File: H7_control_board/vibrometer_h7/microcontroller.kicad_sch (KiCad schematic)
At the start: 34 parts, among them J2 Conn_ARM_SWD_TagConnect_TC203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, J3 Conn_01x04_Socket, Q201 BSS138, Q202 BSS138, SW201 SW_Push, U1 STM32H723VGTx, Y201 24MHz

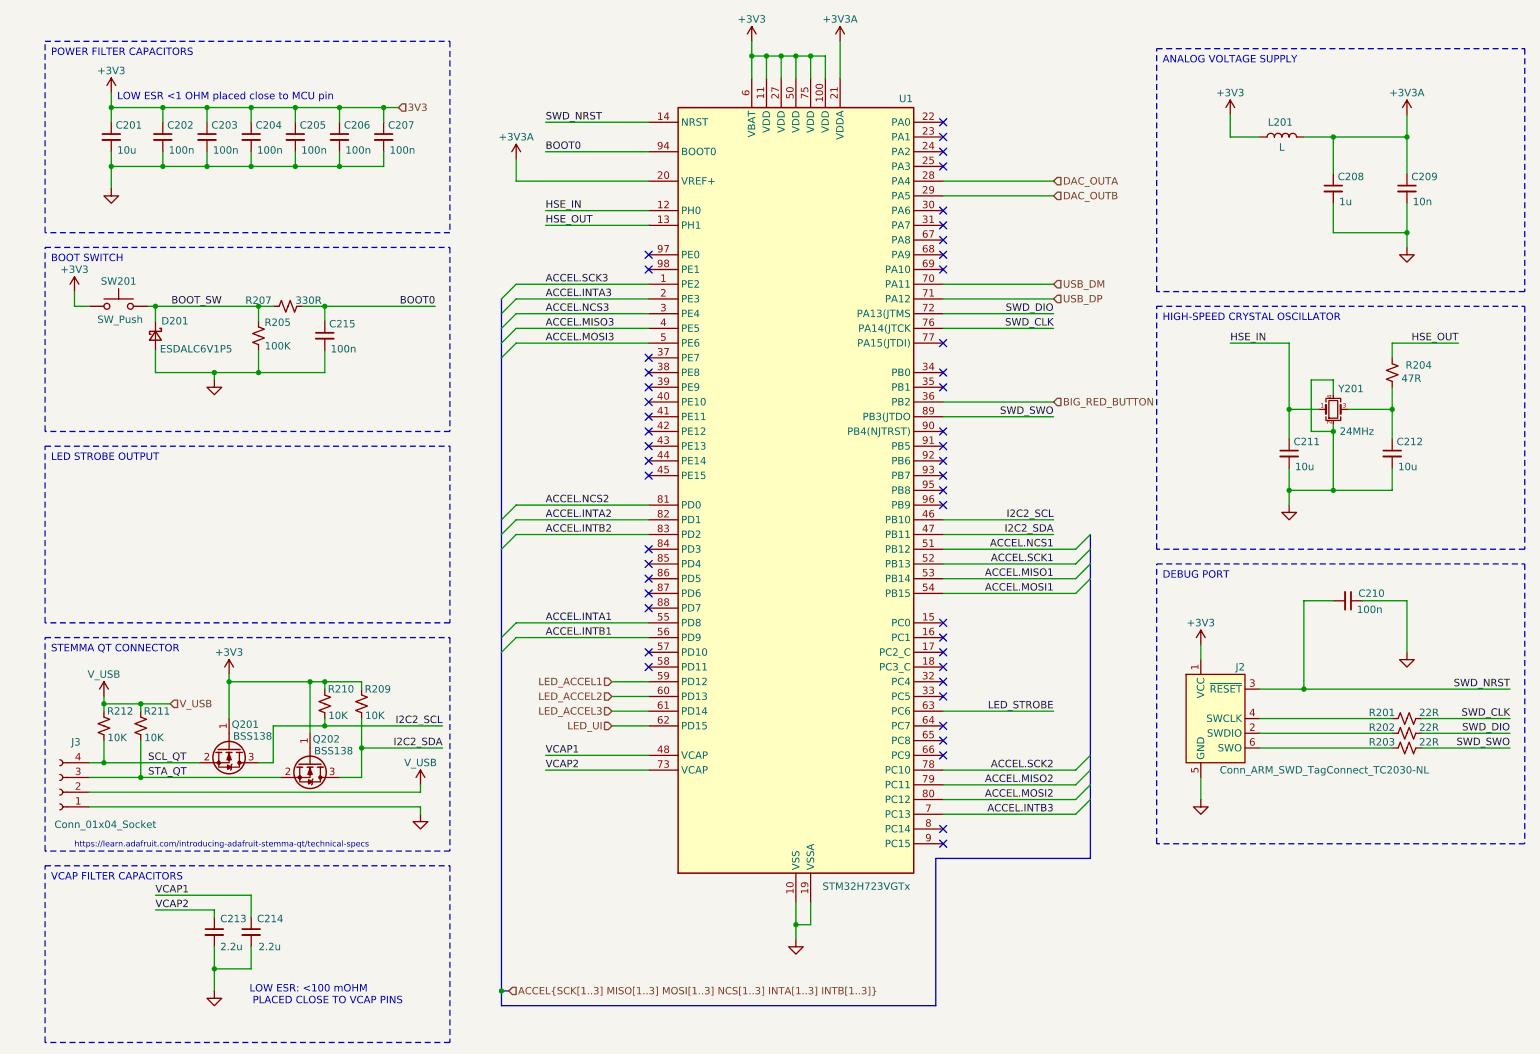
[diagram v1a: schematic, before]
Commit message: adding strobe light to board itself
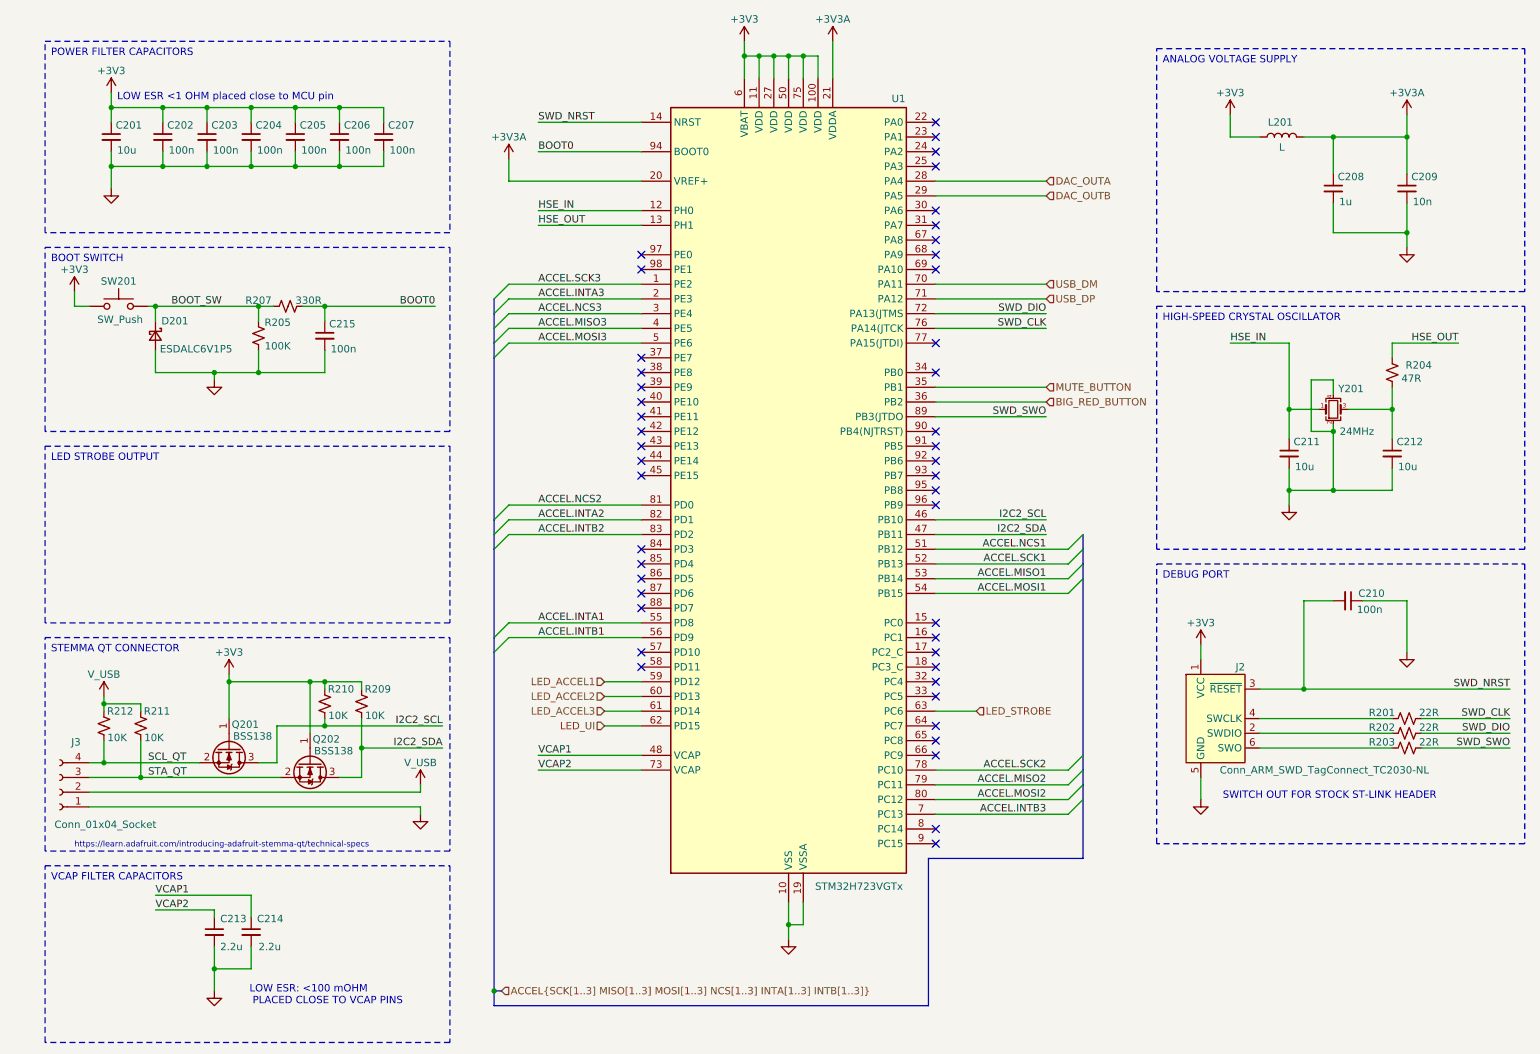
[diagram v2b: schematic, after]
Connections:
- net MUTE_BUTTON: now reaches U1.35 (PB1)
- no-connect marks 47 -> 46
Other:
- note added: "SWITCH OUT FOR STOCK ST-LINK HEADER"
- moved on the sheet: U1

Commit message: worked on audio output stuff, cleaned schematic
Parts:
- removed C210: 100n, symbol Device:C_Small
- removed J2: Conn_ARM_SWD_TagConnect_TC2030-NL, Connector:Tag-Connect_TC2030-IDC-NL_2x03_P1.27mm_Vertical, symbol Connector:Conn_ARM_SWD_TagConnect_TC2030-NL
- added C216, C5: 100n, symbol Device:C_Small
- added J4: Conn_ST_STDC14, symbol Connector:Conn_ST_STDC14
- C211, C212: value 10u -> 12p
- C213, C214: value 2.2u -> 2u2
- L201: value L -> 39n
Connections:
- net +3V3: now also J4.3 (VCC)
- net +3V3A: now also C216.1
- net GND: now also C216.2, C5.1, J4.11 (GNDDetect), J4.5 (GND), J4.7 (GND)
- net SWD_NRST: now also C5.2, J4.12 (~{RST})
- net MUTE_SIGNAL: now reaches U1.30 (PA6)
- net VCP_TX: now reaches U1.92 (PB6)
- net VCP_TX: now also J4.14 (VCP_TX)
- net VCP_RX: now reaches U1.93 (PB7)
- net VCP_RX: now also J4.13 (VCP_RX)
- net at R202.1: now also J4.4 (JTMS/SWDIO)
- net at R201.1: now also J4.6 (JCLK/SWCLK)
- net at R203.1: now also J4.8 (JTDO/SWO)
- net LED_ACCEL1 renamed LED_ACCEL
- net LED_ACCEL2: no longer names the net of U1.60 (PD13)
- net LED_ACCEL3: no longer names the net of U1.61 (PD14)
- no-connect marks 46 -> 47
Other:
- note added: "GPIO HEADER"
- note added: "ST-LINK DEBUG CONNECTOR"
- note removed: "SWITCH OUT FOR STOCK ST-LINK HEADER"
- moved on the sheet: C209

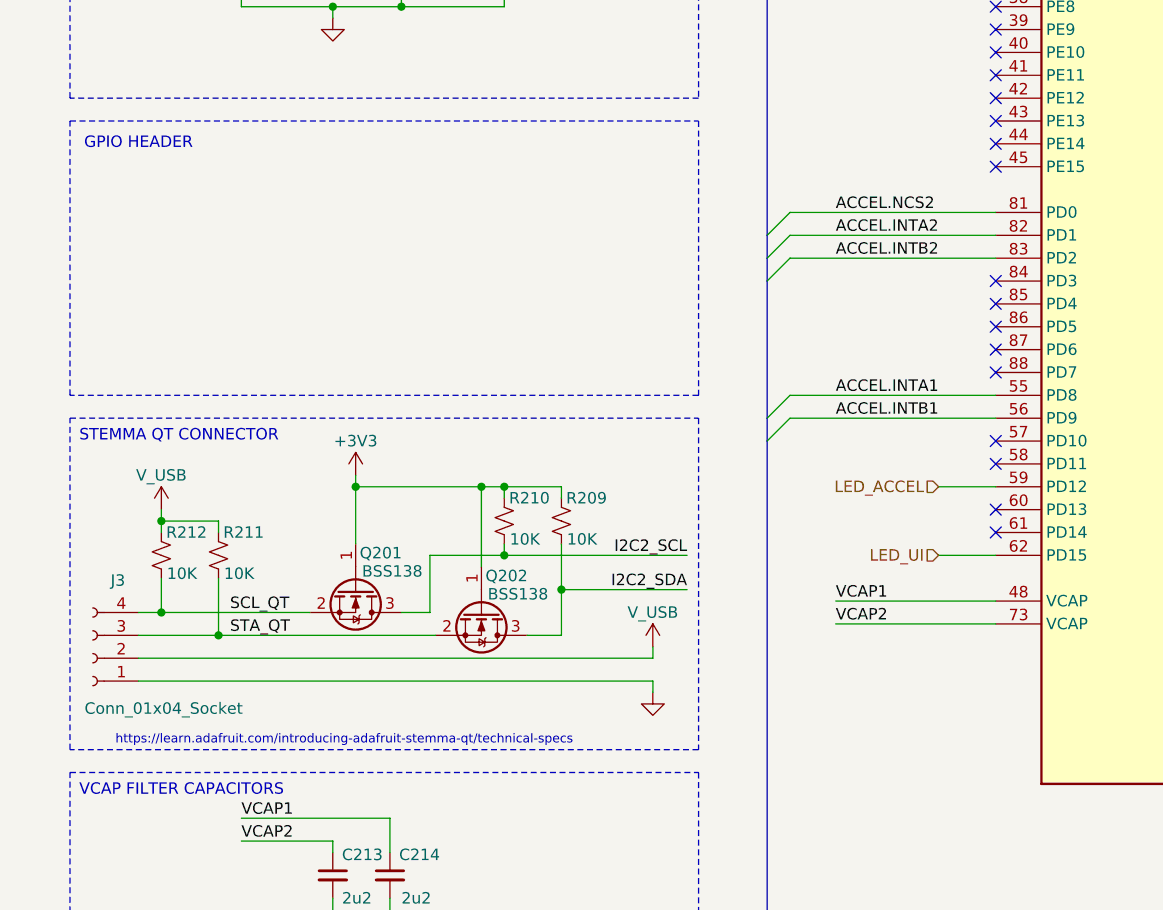
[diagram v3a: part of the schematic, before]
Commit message: met with john to go over schematic. made changes, got rid of some leds...
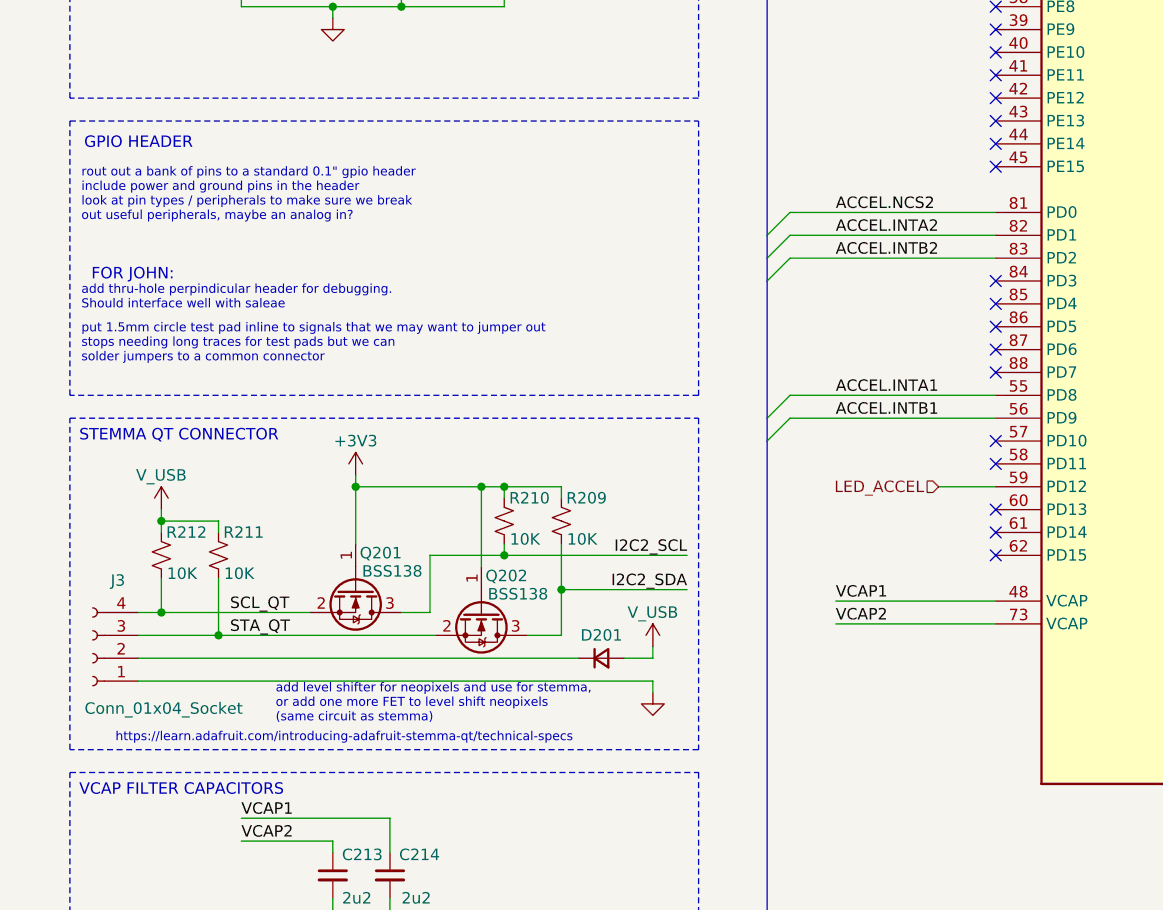
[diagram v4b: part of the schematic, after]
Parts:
- added D201: D_Small, symbol Device:D_Small
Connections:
- net V_USB: now also D201.2 (A); no longer J3.2 (Pin_2)
- net LED_UI: no longer names the net of U1.62 (PD15)
- new net: D201.1 (K), J3.2 (Pin_2)
- no-connect marks 47 -> 48
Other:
- note added: "FOR JOHN:"
- note added: "add level shifter for neopixels and use for stemma, or add one more FET to level shift neopixels (same circuit as stemma)"
- note added: "add thru-hole perpindicular header for debugging. Should interface well with saleae"
- note added: "put 1.5mm circle test pad inline to signals that we may want to jumper out stops needing long traces for test pads but we can solder jumpers to a common connector"
- note added: "rout out a bank of pins to a standard 0.1" gpio header include power and ground pins in the header look at pin types / peripherals to make sure we break out useful peripherals, maybe an analog in?"

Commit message: started part selection
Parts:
- C201, C202, C203, C204, C205, C206, C207, C208, C209, C211, C212, C213, C214, C215, C216, C5: footprint (none) -> Capacitor_SMD:C_0603_1608Metric
- SW201: footprint (none) -> Button_Switch_SMD:SW_Push_1P1T_XKB_TS-1187A; LCSC (none) -> C318884

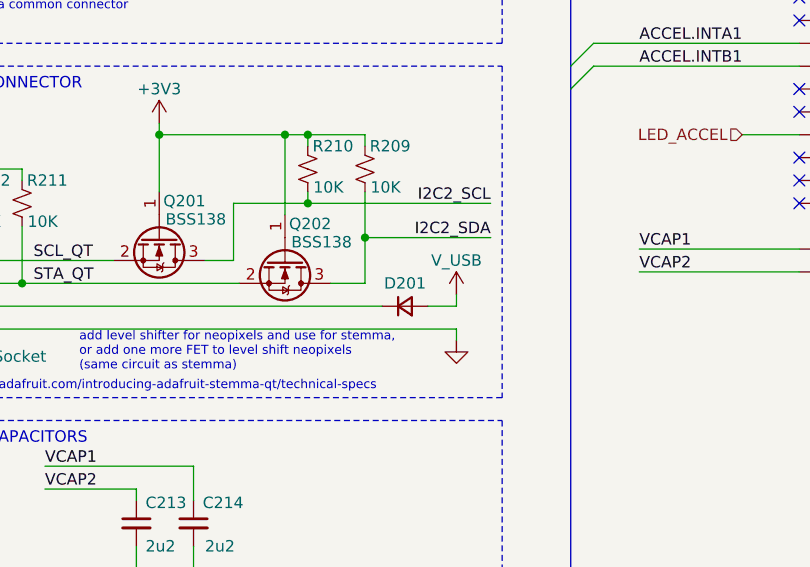
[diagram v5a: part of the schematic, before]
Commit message: component selection, headphone amp circuit specs
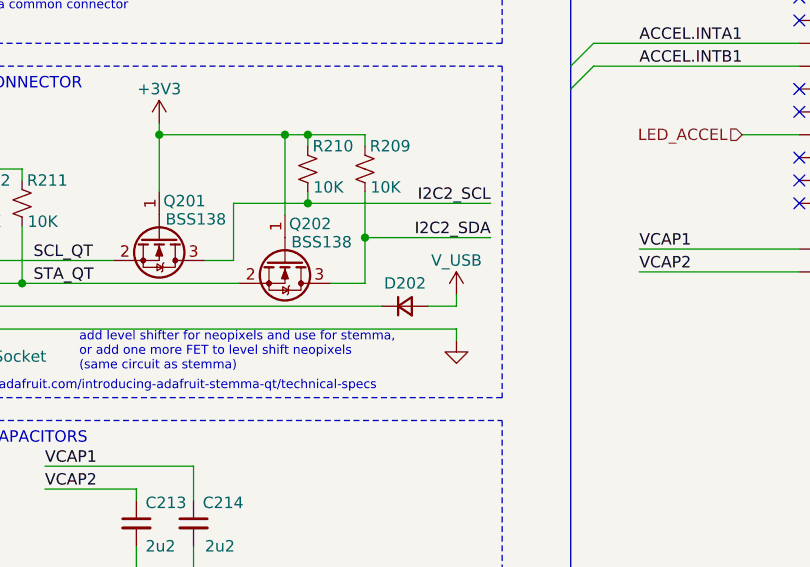
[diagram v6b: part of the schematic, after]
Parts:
- C201: footprint Capacitor_SMD:C_0603_1608Metric -> Capacitor_SMD:C_0805_2012Metric; LCSC (none) -> C15850
- C202, C203, C204, C205, C206, C207, C215, C216, C5: footprint Capacitor_SMD:C_0603_1608Metric -> Capacitor_SMD:C_0402_1005Metric_Pad0.74x0.62mm_HandSolder; LCSC (none) -> C307331
- C208: footprint Capacitor_SMD:C_0603_1608Metric -> Capacitor_SMD:C_0805_2012Metric; LCSC (none) -> C28323
- C213, C214: footprint Capacitor_SMD:C_0603_1608Metric -> Capacitor_SMD:C_0805_2012Metric
- renumbered D201 to D202
